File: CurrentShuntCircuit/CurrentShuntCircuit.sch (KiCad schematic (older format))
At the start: 59 parts, among them J1 Connection, J2 Connection, J3 Debug/UPDI, J4 Screw_Terminal_01x04, J6 ScrewTerminal, J7 Screw_Terminal_01x04, SW1 SW_DIP_x02, U1 TLP172GM, U2 ATtiny1614-SS, U3 INA228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

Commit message: Updated PCB
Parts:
- U4, U7, U8: footprint Package_SO:SOP-8_6.62x9.15mm_P2.54mm -> CurrentShuntCircuit:SMD-8_9.76x6.6x2.54P
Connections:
- net GNDCOMMS is gone; now on net GND2: C15.2, C16.2, C17.2, J7.4 (Pin_4), U6.5 (GND), U7.3 (C), U8.5 (GND)
- net 5VCOMMS: now also C13.1, C17.1, R19.2, R21.2, U4.7 (EN), U4.8 (VCC), U8.7 (EN), U8.8 (VCC)
- net GND: now also C12.1, U7.5 (GND)
- net GND2: now reaches C13.2, U4.5 (GND)
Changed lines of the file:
@@
 Text GLabel 9910 4585 2    50   Input ~ 0
 5VCOMMS
-Text GLabel 9910 5355 2    50   Input ~ 0
-GNDCOMMS
 Wire Wire Line
 	8540 4990 8480 4990
@@
 	8940 5490 8940 5545
 Wire Wire Line
-	8940 5545 9910 5545
+	8940 5545 9570 5545
 Wire Wire Line
 	9910 5070 9910 5545
@@
 check input/output for inverted?
 Wire Wire Line
-	8940 4390 9560 4390
+	8940 4390 9095 4390
 Text GLabel 10720 4085 2    50   Input ~ 0
 5VCOMMS
-Text GLabel 10720 4285 2    50   Input ~ 0
-GNDCOMMS
 Wire Wire Line
 	10375 4085 10520 4085
@@
 F 0 "U8" H 7370 5482 50  0000 C CNN
 F 1 "6N137S(TA)" H 7370 5391 50  0000 C CNN
-F 2 "Package_SO:SOP-8_6.62x9.15mm_P2.54mm" H 7370 4515 50  0001 C CNN
+F 2 "CurrentShuntCircuit:SMD-8_9.76x6.6x2.54P" H 7370 4515 50  0001 C CNN
 F 3 "https://datasheet.lcsc.com/lcsc/1811091924_Everlight-Elec-6N137S-TA_C16496.pdf" H 6520 5565 50  0001 C CNN
 F 4 "C16496" H 7370 5015 50  0001 C CNN "LCSCStockCode"
@@
 Connection ~ 7705 4815
 Wire Wire Line
-	7705 4815 7920 4815
+	7705 4815 7815 4815
 Wire Wire Line
 	8480 4990 8480 4940
@@
 F 0 "U4" H 7350 6512 50  0000 C CNN
 F 1 "6N137S(TA)" H 7350 6421 50  0000 C CNN
-F 2 "Package_SO:SOP-8_6.62x9.15mm_P2.54mm" H 7350 5545 50  0001 C CNN
+F 2 "CurrentShuntCircuit:SMD-8_9.76x6.6x2.54P" H 7350 5545 50  0001 C CNN
 F 3 "https://datasheet.lcsc.com/lcsc/1811091924_Everlight-Elec-6N137S-TA_C16496.pdf" H 6500 6595 50  0001 C CNN
 F 4 "C16496" H 7350 6045 50  0001 C CNN "LCSCStockCode"
@@
 $EndComp
 Wire Wire Line
-	7920 5215 8150 5215
-Wire Wire Line
-	8150 5215 8150 5545
-Wire Wire Line
-	8150 5545 8940 5545
+	7920 5215 8045 5215
 Connection ~ 7920 5215
-Connection ~ 8940 5545
 Wire Wire Line
 	7650 5945 7755 5945
@@
 F 0 "U7" H 7370 3413 50  0000 C CNN
 F 1 "6N137S(TA)" H 7370 3504 50  0000 C CNN
-F 2 "Package_SO:SOP-8_6.62x9.15mm_P2.54mm" H 7370 3380 50  0001 C CNN
+F 2 "CurrentShuntCircuit:SMD-8_9.76x6.6x2.54P" H 7370 3380 50  0001 C CNN
 F 3 "https://datasheet.lcsc.com/lcsc/1811091924_Everlight-Elec-6N137S-TA_C16496.pdf" H 6520 4430 50  0001 C CNN
 F 4 "C16496" H 7370 3880 50  0001 C CNN "LCSCStockCode"
@@
 Wire Wire Line
 	8395 4790 8540 4790
-Text GLabel 7870 3680 2    50   Input ~ 0
-GNDCOMMS
-Wire Wire Line
-	7870 3680 7670 3680
 $Comp
 L Device:R_Small R12
@@
 	-1   0    0    1
 $EndComp
-Text Notes 6245 3610 0    50   ~ 0
+Text Notes 6285 4255 0    50   ~ 0
 Pull up may \nbe not needed
 $Comp
@@
 	6770 3880 6770 3680
 Wire Wire Line
-	6770 3680 7070 3680
+	6770 3680 7040 3680
 Wire Wire Line
 	7070 3980 7070 4020
@@
 Text GLabel 1655 6960 0    59   Input ~ 0
 SDA
+$Comp
+L power:GND #PWR0106
+U 1 1 6220C629
+P 6920 3420
+F 0 "#PWR0106" H 6920 3170 50  0001 C CNN
+F 1 "GND" H 6925 3247 50  0000 C CNN
+F 2 "" H 6920 3420 50  0001 C CNN
+F 3 "" H 6920 3420 50  0001 C CNN
+	1    6920 3420
+	1    0    0    -1
+$EndComp
+Wire Wire Line
+	7040 3680 7040 3420
+Wire Wire Line
+	7040 3420 6920 3420
+Connection ~ 7040 3680
+Wire Wire Line
+	7040 3680 7070 3680
+Wire Wire Line
+	7890 6245 7950 6245
+Connection ~ 7890 6245
+$Comp
+L power:GND2 #PWR0107
+U 1 1 622243AB
+P 9570 5545
+F 0 "#PWR0107" H 9570 5295 50  0001 C CNN
+F 1 "GND2" H 9575 5372 50  0000 C CNN
+F 2 "" H 9570 5545 50  0001 C CNN
+F 3 "" H 9570 5545 50  0001 C CNN
+	1    9570 5545
+	1    0    0    -1
+$EndComp
+Connection ~ 9570 5545
+Wire Wire Line
+	9570 5545 9910 5545
+$Comp
+L power:GND2 #PWR0108
+U 1 1 62224F8A
+P 7810 3680
+F 0 "#PWR0108" H 7810 3430 50  0001 C CNN
+F 1 "GND2" V 7815 3552 50  0000 R CNN
+F 2 "" H 7810 3680 50  0001 C CNN
+F 3 "" H 7810 3680 50  0001 C CNN
+	1    7810 3680
+	0    -1   -1   0
+$EndComp
+Wire Wire Line
+	7810 3680 7670 3680
+$Comp
+L power:GND2 #PWR0109
+U 1 1 622257B5
+P 10720 4285
+F 0 "#PWR0109" H 10720 4035 50  0001 C CNN
+F 1 "GND2" H 10725 4112 50  0000 C CNN
+F 2 "" H 10720 4285 50  0001 C CNN
+F 3 "" H 10720 4285 50  0001 C CNN
+	1    10720 4285
+	1    0    0    -1
+$EndComp
+$Comp
+L power:GND2 #PWR0110
+U 1 1 62225E97
+P 7950 6245
+F 0 "#PWR0110" H 7950 5995 50  0001 C CNN
+F 1 "GND2" H 7955 6072 50  0000 C CNN
+F 2 "" H 7950 6245 50  0001 C CNN
+F 3 "" H 7950 6245 50  0001 C CNN
+	1    7950 6245
+	1    0    0    -1
+$EndComp
+$Comp
+L power:GND2 #PWR0111
+U 1 1 622264D0
+P 8045 5215
+F 0 "#PWR0111" H 8045 4965 50  0001 C CNN
+F 1 "GND2" H 8050 5042 50  0000 C CNN
+F 2 "" H 8045 5215 50  0001 C CNN
+F 3 "" H 8045 5215 50  0001 C CNN
+	1    8045 5215
+	1    0    0    -1
+$EndComp
+Wire Wire Line
+	9095 4390 9095 4340
+Wire Wire Line
+	9095 4340 8315 4340
+Wire Wire Line
+	7815 4340 7815 4815
+Connection ~ 9095 4390
+Wire Wire Line
+	9095 4390 9560 4390
+Connection ~ 7815 4815
+Wire Wire Line
+	7815 4815 7920 4815
+Wire Wire Line
+	8315 5845 8315 4340
+Connection ~ 8315 5845
+Connection ~ 8315 4340
+Wire Wire Line
+	8315 4340 7815 4340
 $EndSCHEMATC

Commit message: Part rotation fix
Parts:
- C1, C16, C2, C7: LCSCStockCode C28323 -> C215803; PartNumber CL21B105KBFNNNE -> 0805B105K500NT
- U4, U7, U8: JLCPCBRotation (none) -> 180; PartNumber (none) -> 6N137S(TA)
- U6: JLCPCBRotation (none) -> 270
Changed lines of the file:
@@
 F 2 "Capacitor_SMD:C_0805_2012Metric" H 4218 1055 50  0001 C CNN
 F 3 "~" H 4180 1205 50  0001 C CNN
-F 4 "C28323" H 4180 1205 50  0001 C CNN "LCSCStockCode"
-F 5 "CL21B105KBFNNNE" H 4180 1205 50  0001 C CNN "PartNumber"
+F 4 "C215803" H 4180 1205 50  0001 C CNN "LCSCStockCode"
+F 5 "0805B105K500NT" H 4180 1205 50  0001 C CNN "PartNumber"
 	1    4180 1205
 	1    0    0    -1
@@
 F 2 "Capacitor_SMD:C_0805_2012Metric" H 2658 3760 50  0001 C CNN
 F 3 "~" H 2620 3910 50  0001 C CNN
-F 4 "C28323" H 2620 3910 50  0001 C CNN "LCSCStockCode"
-F 5 "CL21B105KBFNNNE" H 2620 3910 50  0001 C CNN "PartNumber"
+F 4 "C215803" H 2620 3910 50  0001 C CNN "LCSCStockCode"
+F 5 "0805B105K500NT" H 2620 3910 50  0001 C CNN "PartNumber"
 	1    2620 3910
 	1    0    0    -1
@@
 F 3 "~" H 8815 985 50  0001 C CNN
 F 4 "" H 8815 985 50  0001 C CNN "JLC"
-F 5 "CL21B105KBFNNNE" H 8815 985 50  0001 C CNN "PartNumber"
-F 6 "C28323" H 8815 985 50  0001 C CNN "LCSCStockCode"
+F 5 "0805B105K500NT" H 8815 985 50  0001 C CNN "PartNumber"
+F 6 "C215803" H 8815 985 50  0001 C CNN "LCSCStockCode"
 	1    8815 985
 	1    0    0    -1
@@
 F 4 "C6855" H 8940 4890 50  0001 C CNN "LCSCStockCode"
 F 5 "SP485EEN-L/TR" H 8940 4890 50  0001 C CNN "PartNumber"
+F 6 "270" H 8940 4890 50  0001 C CNN "JLCPCBRotation"
 	1    8940 4890
 	1    0    0    -1
@@
 F 2 "Capacitor_SMD:C_0805_2012Metric" H 10520 4185 50  0001 C CNN
 F 3 "~" H 10520 4185 50  0001 C CNN
-F 4 "C28323" H 10520 4185 50  0001 C CNN "LCSCStockCode"
-F 5 "CL21B105KBFNNNE" H 10520 4185 50  0001 C CNN "PartNumber"
+F 4 "C215803" H 10520 4185 50  0001 C CNN "LCSCStockCode"
+F 5 "0805B105K500NT" H 10520 4185 50  0001 C CNN "PartNumber"
 	1    10520 4185
 	1    0    0    -1
@@
 F 3 "https://datasheet.lcsc.com/lcsc/1811091924_Everlight-Elec-6N137S-TA_C16496.pdf" H 6520 5565 50  0001 C CNN
 F 4 "C16496" H 7370 5015 50  0001 C CNN "LCSCStockCode"
+F 5 "180" H 7370 5015 50  0001 C CNN "JLCPCBRotation"
+F 6 "6N137S(TA)" H 7370 5015 50  0001 C CNN "PartNumber"
 	1    7370 5015
 	1    0    0    -1
@@
 F 3 "https://datasheet.lcsc.com/lcsc/1811091924_Everlight-Elec-6N137S-TA_C16496.pdf" H 6500 6595 50  0001 C CNN
 F 4 "C16496" H 7350 6045 50  0001 C CNN "LCSCStockCode"
+F 5 "180" H 7350 6045 50  0001 C CNN "JLCPCBRotation"
+F 6 "6N137S(TA)" H 7350 6045 50  0001 C CNN "PartNumber"
 	1    7350 6045
 	1    0    0    -1
@@
 F 3 "https://datasheet.lcsc.com/lcsc/1811091924_Everlight-Elec-6N137S-TA_C16496.pdf" H 6520 4430 50  0001 C CNN
 F 4 "C16496" H 7370 3880 50  0001 C CNN "LCSCStockCode"
+F 5 "180" H 7370 3880 50  0001 C CNN "JLCPCBRotation"
+F 6 "6N137S(TA)" H 7370 3880 50  0001 C CNN "PartNumber"
 	1    7370 3880
 	-1   0    0    1

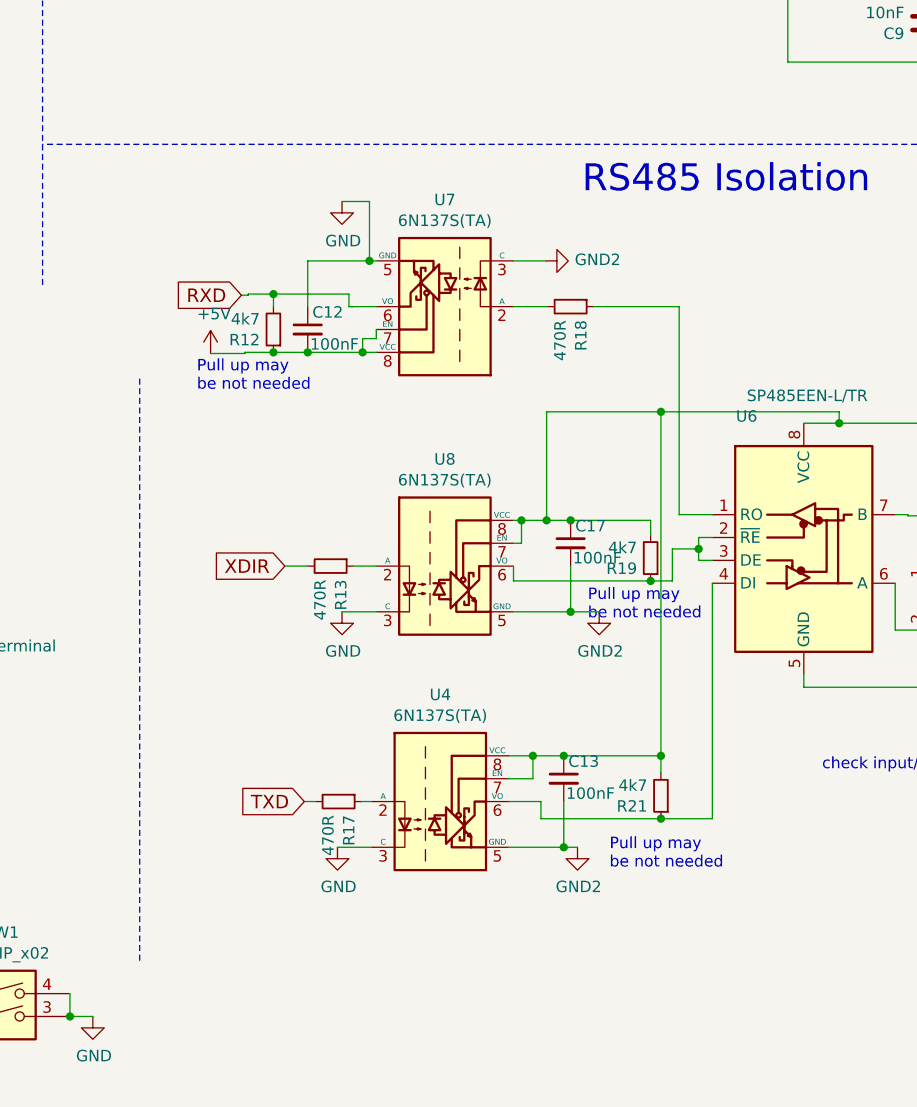
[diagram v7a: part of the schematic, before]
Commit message: Change to use smaller part  H11L1S(TA)
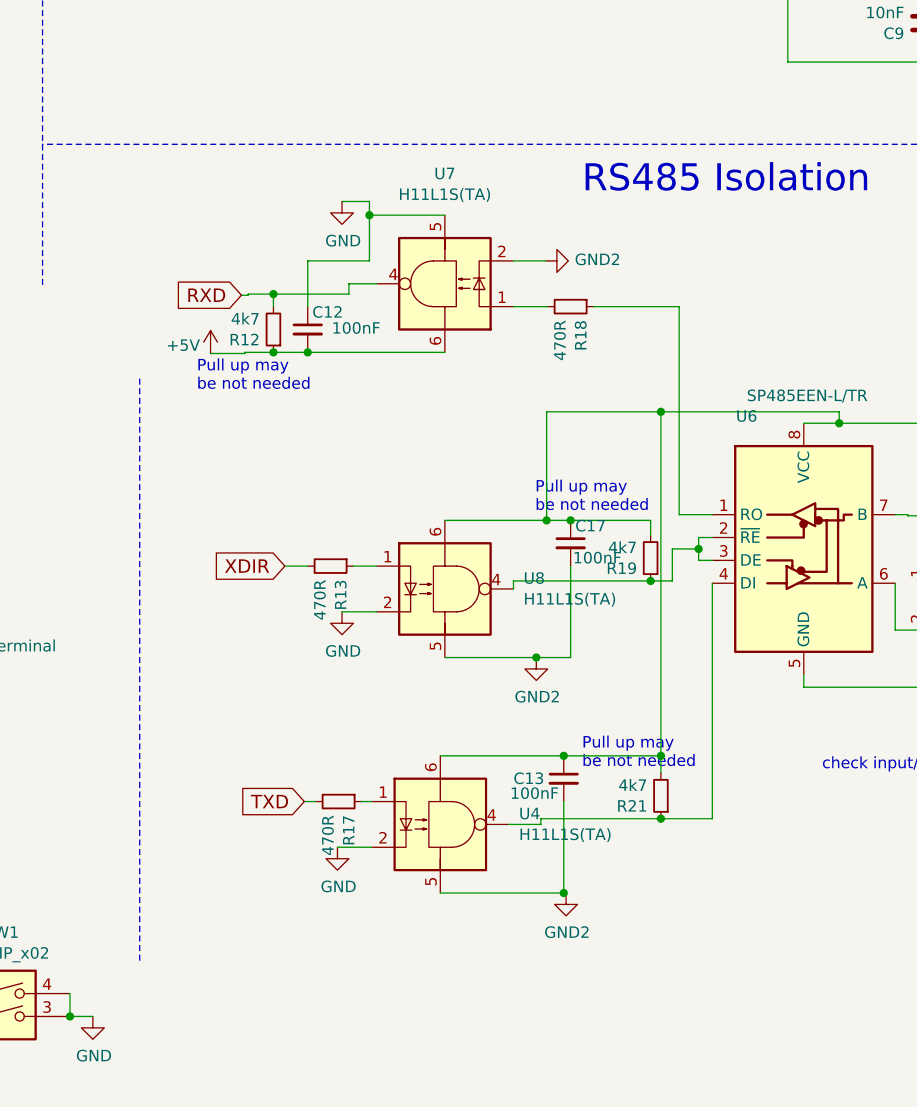
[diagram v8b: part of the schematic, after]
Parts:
- removed U4, U7, U8: 6N137S(TA), CurrentShuntCircuit:SMD-8_9.76x6.6x2.54P, symbol Isolator:6N137
- added U4, U7, U8: H11L1S(TA), CurrentShuntCircuit:SMD-6_6.5x7.1x2.54P, symbol Isolator:H11L1
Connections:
- net +5V: now also U7.6
- net 5VCOMMS: now also U4.6, U8.6
- net GND: now also U4.2, U7.5, U8.2
- net GND2: now also U4.5, U7.2, U8.5
- net RXD: now also U7.4
- net at R19.1, U6.2 (~RE), U6.3 (DE): now also U8.4
- net at R21.1, U6.4 (DI): now also U4.4
- net at R13.1: now also U8.1
- net at R17.1: now also U4.1
- net at R18.2: now also U7.1
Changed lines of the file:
@@
 	5610 3785 5610 600
-Wire Notes Line
-	6960 3880 6970 3880
 Wire Notes Line
 	6035 4195 6035 6745
@@
 Connection ~ 10520 4285
 $Comp
-L Isolator:6N137 U8
-U 1 1 6200C0F6
-P 7370 5015
-F 0 "U8" H 7370 5482 50  0000 C CNN
-F 1 "6N137S(TA)" H 7370 5391 50  0000 C CNN
-F 2 "CurrentShuntCircuit:SMD-8_9.76x6.6x2.54P" H 7370 4515 50  0001 C CNN
-F 3 "https://datasheet.lcsc.com/lcsc/1811091924_Everlight-Elec-6N137S-TA_C16496.pdf" H 6520 5565 50  0001 C CNN
-F 4 "C16496" H 7370 5015 50  0001 C CNN "LCSCStockCode"
-F 5 "180" H 7370 5015 50  0001 C CNN "JLCPCBRotation"
-F 6 "6N137S(TA)" H 7370 5015 50  0001 C CNN "PartNumber"
-	1    7370 5015
-	1    0    0    -1
-$EndComp
-$Comp
 L Device:C_Small C17
 U 1 1 6200CDDE
@@
 	1    0    0    -1
 $EndComp
-Wire Wire Line
-	7670 4815 7705 4815
-Wire Wire Line
-	7670 5215 7920 5215
-Wire Wire Line
-	7920 5215 7920 5015
 $Comp
 L Jumper:SolderJumper_2_Bridged JP1
@@
 	6920 5215 7070 5215
 Wire Wire Line
-	7670 4915 7705 4915
-Wire Wire Line
-	7705 4915 7705 4815
-Connection ~ 7705 4815
-Wire Wire Line
-	7705 4815 7815 4815
-Wire Wire Line
 	8480 4990 8480 4940
-Wire Wire Line
-	7670 5015 7670 5080
 Wire Wire Line
 	7670 5080 8270 5080
@@
 Wire Wire Line
 	8480 4940 8480 4890
-$Comp
-L Isolator:6N137 U4
-U 1 1 62088B64
-P 7350 6045
-F 0 "U4" H 7350 6512 50  0000 C CNN
-F 1 "6N137S(TA)" H 7350 6421 50  0000 C CNN
-F 2 "CurrentShuntCircuit:SMD-8_9.76x6.6x2.54P" H 7350 5545 50  0001 C CNN
-F 3 "https://datasheet.lcsc.com/lcsc/1811091924_Everlight-Elec-6N137S-TA_C16496.pdf" H 6500 6595 50  0001 C CNN
-F 4 "C16496" H 7350 6045 50  0001 C CNN "LCSCStockCode"
-F 5 "180" H 7350 6045 50  0001 C CNN "JLCPCBRotation"
-F 6 "6N137S(TA)" H 7350 6045 50  0001 C CNN "PartNumber"
-	1    7350 6045
-	1    0    0    -1
-$EndComp
-Wire Wire Line
-	7920 5215 8045 5215
-Connection ~ 7920 5215
-Wire Wire Line
-	7650 5945 7755 5945
-Wire Wire Line
-	7755 5945 7755 5845
-Wire Wire Line
-	7755 5845 7650 5845
 $Comp
 L Device:C_Small C13
 U 1 1 6209A5DA
 P 7890 5945
-F 0 "C13" H 7910 6020 50  0000 L CNN
-F 1 "100nF" H 7900 5880 50  0000 L CNN
+F 0 "C13" H 7670 5945 50  0000 L CNN
+F 1 "100nF" H 7655 5880 50  0000 L CNN
 F 2 "Capacitor_SMD:C_0805_2012Metric" H 7928 5795 50  0001 C CNN
 F 3 "" H 7890 5945 50  0001 C CNN
@@
 	1    0    0    -1
 $EndComp
-Wire Wire Line
-	7755 5845 7890 5845
-Connection ~ 7755 5845
-Wire Wire Line
-	7650 6245 7890 6245
-Wire Wire Line
-	7890 6245 7890 6045
-Wire Wire Line
-	7650 6045 7790 6045
-Wire Wire Line
-	7790 6045 7790 6120
 Wire Wire Line
 	7790 6120 8315 6120
@@
 	8315 5845 7890 5845
 Connection ~ 7890 5845
-Text Notes 8090 6345 0    50   ~ 0
+Text Notes 7970 5905 0    50   ~ 0
 Pull up may \nbe not needed
 $Comp
@@
 	8270 4815 8270 4880
 Connection ~ 7920 4815
-Text Notes 7995 5255 0    50   ~ 0
+Text Notes 7765 4785 0    50   ~ 0
 Pull up may \nbe not needed
-$Comp
-L Isolator:6N137 U7
-U 1 1 620E0883
-P 7370 3880
-F 0 "U7" H 7370 3413 50  0000 C CNN
-F 1 "6N137S(TA)" H 7370 3504 50  0000 C CNN
-F 2 "CurrentShuntCircuit:SMD-8_9.76x6.6x2.54P" H 7370 3380 50  0001 C CNN
-F 3 "https://datasheet.lcsc.com/lcsc/1811091924_Everlight-Elec-6N137S-TA_C16496.pdf" H 6520 4430 50  0001 C CNN
-F 4 "C16496" H 7370 3880 50  0001 C CNN "LCSCStockCode"
-F 5 "180" H 7370 3880 50  0001 C CNN "JLCPCBRotation"
-F 6 "6N137S(TA)" H 7370 3880 50  0001 C CNN "PartNumber"
-	1    7370 3880
-	-1   0    0    1
-$EndComp
 $Comp
 L Device:R_Small R18
@@
 P 6770 3980
 F 0 "C12" H 6790 4055 50  0000 L CNN
-F 1 "100nF" H 6780 3915 50  0000 L CNN
+F 1 "100nF" H 6875 3985 50  0000 L CNN
 F 2 "Capacitor_SMD:C_0805_2012Metric" H 6808 3830 50  0001 C CNN
 F 3 "" H 6770 3980 50  0001 C CNN
@@
 $EndComp
 Wire Wire Line
-	7070 4080 7010 4080
-Wire Wire Line
 	6770 4080 6620 4080
 Connection ~ 6770 4080
@@
 Wire Wire Line
 	6770 3680 7040 3680
-Wire Wire Line
-	7070 3980 7070 4020
-Wire Wire Line
-	7070 4020 7010 4020
-Wire Wire Line
-	7010 4020 7010 4080
-Connection ~ 7010 4080
-Wire Wire Line
-	7010 4080 6770 4080
-Wire Wire Line
-	7070 3880 6950 3880
-Wire Wire Line
-	6950 3880 6950 3825
 Wire Wire Line
 	6950 3825 6620 3825
@@
 P 6345 4085
 F 0 "#PWR018" H 6345 3935 50  0001 C CNN
-F 1 "+5V" H 6360 4258 50  0000 C CNN
+F 1 "+5V" H 6225 4120 50  0000 C CNN
 F 2 "" H 6345 4085 50  0001 C CNN
 F 3 "" H 6345 4085 50  0001 C CNN
@@
 $EndComp
 Wire Wire Line
-	7040 3680 7040 3420
-Wire Wire Line
 	7040 3420 6920 3420
-Connection ~ 7040 3680
-Wire Wire Line
-	7040 3680 7070 3680
-Wire Wire Line
-	7890 6245 7950 6245
-Connection ~ 7890 6245
 $Comp
 L power:GND2 #PWR0107
@@
 L power:GND2 #PWR0110
 U 1 1 62225E97
-P 7950 6245
-F 0 "#PWR0110" H 7950 5995 50  0001 C CNN
-F 1 "GND2" H 7955 6072 50  0000 C CNN
-F 2 "" H 7950 6245 50  0001 C CNN
-F 3 "" H 7950 6245 50  0001 C CNN
-	1    7950 6245
+P 7900 6445
+F 0 "#PWR0110" H 7900 6195 50  0001 C CNN
+F 1 "GND2" H 7905 6272 50  0000 C CNN
+F 2 "" H 7900 6445 50  0001 C CNN
+F 3 "" H 7900 6445 50  0001 C CNN
+	1    7900 6445
 	1    0    0    -1
 $EndComp
@@
 L power:GND2 #PWR0111
 U 1 1 622264D0
-P 8045 5215
-F 0 "#PWR0111" H 8045 4965 50  0001 C CNN
-F 1 "GND2" H 8050 5042 50  0000 C CNN
-F 2 "" H 8045 5215 50  0001 C CNN
-F 3 "" H 8045 5215 50  0001 C CNN
-	1    8045 5215
+P 7770 5415
+F 0 "#PWR0111" H 7770 5165 50  0001 C CNN
+F 1 "GND2" H 7775 5242 50  0000 C CNN
+F 2 "" H 7770 5415 50  0001 C CNN
+F 3 "" H 7770 5415 50  0001 C CNN
+	1    7770 5415
 	1    0    0    -1
 $EndComp
@@
 Wire Wire Line
 	8315 4340 7815 4340
+$Comp
+L Isolator:H11L1 U4
+U 1 1 620B10DA
+P 7350 6145
+F 0 "U4" H 7694 6191 50  0000 L CNN
+F 1 "H11L1S(TA)" H 7694 6100 50  0000 L CNN
+F 2 "CurrentShuntCircuit:SMD-6_6.5x7.1x2.54P" H 7260 6145 50  0001 C CNN
+F 3 "https://datasheet.lcsc.com/lcsc/1810111530_Everlight-Elec-H11L1S-TA_C78589.pdf" H 7260 6145 50  0001 C CNN
+F 4 "C78589" H 7350 6145 50  0001 C CNN "LCSCStockCode"
+	1    7350 6145
+	1    0    0    -1
+$EndComp
+Wire Wire Line
+	7350 6445 7890 6445
+Wire Wire Line
+	7650 6145 7790 6145
+Wire Wire Line
+	7790 6145 7790 6120
+Wire Wire Line
+	7890 6045 7890 6445
+Connection ~ 7890 6445
+Wire Wire Line
+	7890 6445 7900 6445
+Wire Wire Line
+	7350 5845 7890 5845
+$Comp
+L Isolator:H11L1 U8
+U 1 1 620E7341
+P 7370 5115
+F 0 "U8" H 7714 5161 50  0000 L CNN
+F 1 "H11L1S(TA)" H 7714 5070 50  0000 L CNN
+F 2 "CurrentShuntCircuit:SMD-6_6.5x7.1x2.54P" H 7280 5115 50  0001 C CNN
+F 3 "https://datasheet.lcsc.com/lcsc/1810111530_Everlight-Elec-H11L1S-TA_C78589.pdf" H 7280 5115 50  0001 C CNN
+F 4 "C78589" H 7370 5115 50  0001 C CNN "LCSCStockCode"
+	1    7370 5115
+	1    0    0    -1
+$EndComp
+Wire Wire Line
+	7370 5415 7770 5415
+Wire Wire Line
+	7770 5415 7920 5415
+Wire Wire Line
+	7920 5015 7920 5415
+Connection ~ 7770 5415
+Wire Wire Line
+	7670 5115 7670 5080
+Wire Wire Line
+	7370 4815 7815 4815
+$Comp
+L Isolator:H11L1 U7
+U 1 1 62116ED1
+P 7370 3780
+F 0 "U7" H 7370 3299 50  0000 C CNN
+F 1 "H11L1S(TA)" H 7370 3390 50  0000 C CNN
+F 2 "CurrentShuntCircuit:SMD-6_6.5x7.1x2.54P" H 7280 3780 50  0001 C CNN
+F 3 "https://datasheet.lcsc.com/lcsc/1810111530_Everlight-Elec-H11L1S-TA_C78589.pdf" H 7280 3780 50  0001 C CNN
+F 4 "C78589" H 7370 3780 50  0001 C CNN "LCSCStockCode"
+	1    7370 3780
+	-1   0    0    1
+$EndComp
+Wire Wire Line
+	7040 3480 7370 3480
+Wire Wire Line
+	7040 3420 7040 3480
+Connection ~ 7040 3480
+Wire Wire Line
+	7040 3480 7040 3680
+Wire Wire Line
+	7070 3780 6950 3780
+Wire Wire Line
+	6950 3780 6950 3825
+Wire Wire Line
+	6770 4080 7370 4080
 $EndSCHEMATC
